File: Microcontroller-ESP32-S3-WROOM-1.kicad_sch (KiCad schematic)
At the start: 8 parts, among them SW1 SW_Push, U1 ESP32-S3-WROOM-1

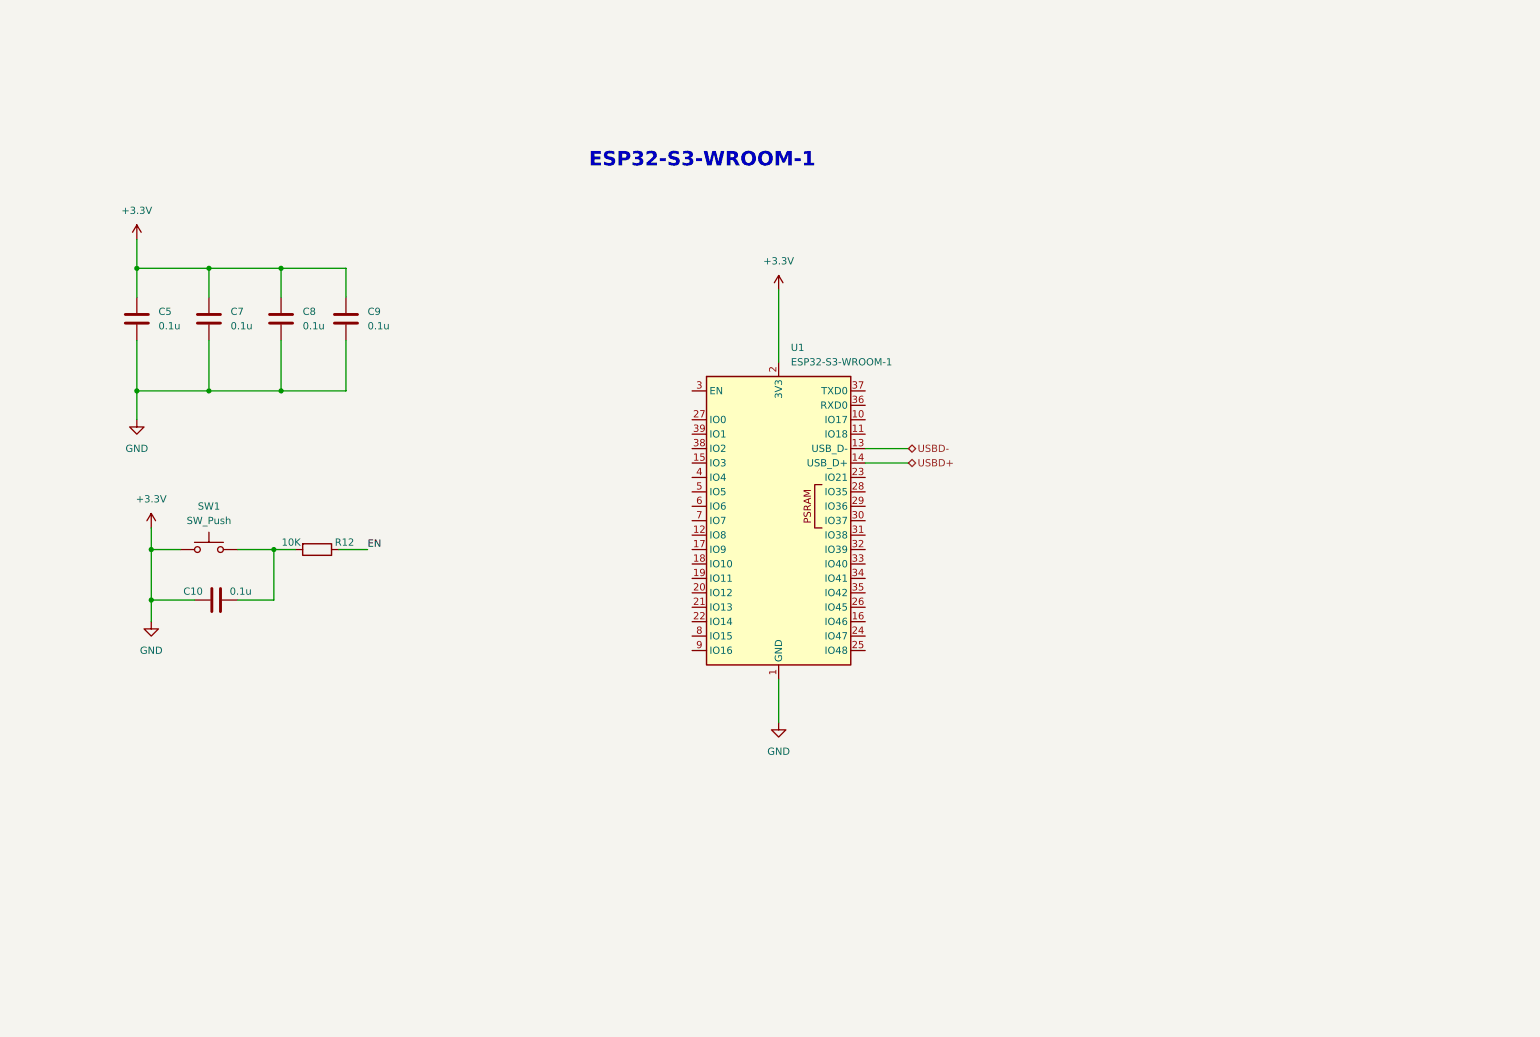
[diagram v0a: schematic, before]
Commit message: feat(schematic): replace capacitor with LED component
Update the ESP32-S3 schematic by replacing a generic capacitor symbol with a specific LED component (LTST-C170KRKT), including updated footprints, properties, and pin configurations.
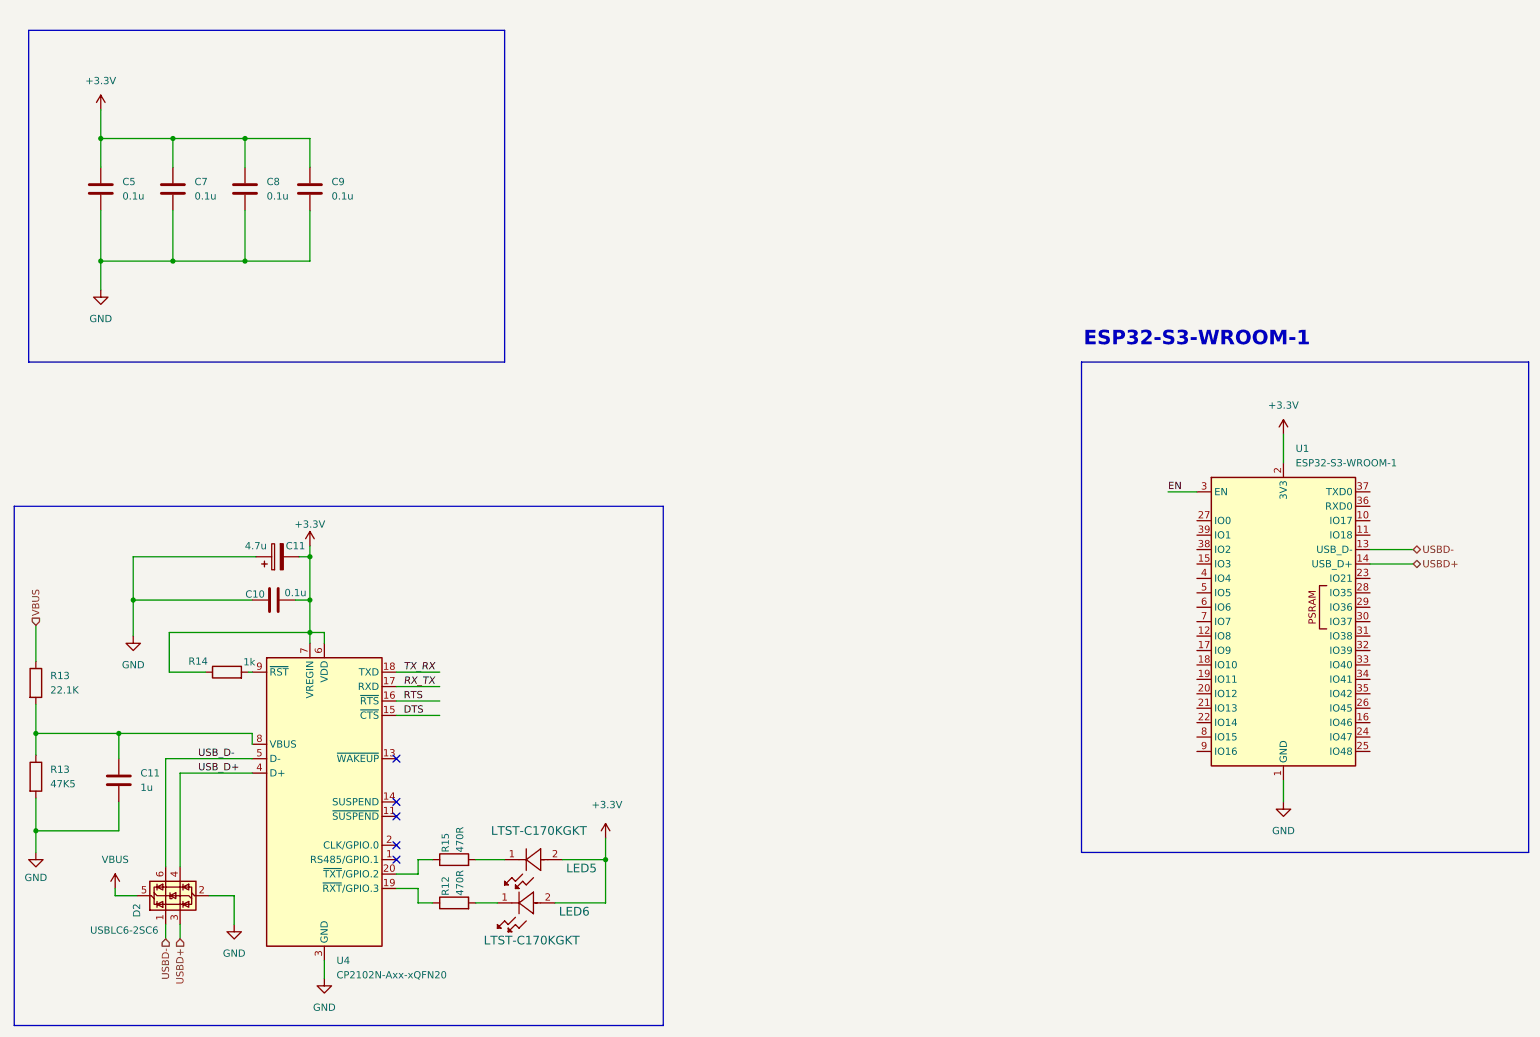
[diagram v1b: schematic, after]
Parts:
- removed SW1: SW_Push, symbol Switch:SW_Push
- added C11: 4.7u, FootPrints:CAPMP3216X180N, symbol Device:C_Polarized
- added C11: 1u, Capacitor_SMD:C_0805_2012Metric, symbol Device:C
- added D2: USBLC6-2SC6, Package_TO_SOT_SMD:SOT-23-6, symbol Power_Protection:USBLC6-2SC6
- added LED5, LED6: LTST-C170KGKT, LED_SMD:LED_0805_2012Metric, symbol 2025-07-01_05-07-46:LTST-C170KRKT
- added R13: 22.1K, Resistor_SMD:R_0805_2012Metric, symbol Device:R
- added R13: 47K5, Resistor_SMD:R_0805_2012Metric, symbol Device:R
- added R14: 1k, Resistor_SMD:R_0805_2012Metric, symbol Device:R
- added R15: 470R, Resistor_SMD:R_0201_0603Metric, symbol Device:R
- added U4: CP2102N-Axx-xQFN20, FootPrints:WFQFN-20, symbol Interface_USB:CP2102N-Axx-xQFN20
- R12: value 10K -> 470R; footprint Resistor_SMD:R_0805_2012Metric -> Resistor_SMD:R_0201_0603Metric; Distributor_link_1 https://eu.mouser.com/ProductDetail/Vishay/CRCW121810K0FKEK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 -> https://eu.mouser.com/ProductDetail/Vishay/CRCW0603470RFKEB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; Distributor_link_2 https://www.digikey.com/en/products/detail/vishay-dale/CRCW121810K0FKEK/28261299 -> https://www.digikey.com/en/products/detail/vishay-dale/CRCW0603470RFKEBC/7925149; LCSC C2144629 -> C4553842; Manufacturer CRCW121810K0FKEK -> Vishay; Manufacturer_part_number Vishay -> CRCW0603470RFKEBC
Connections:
- net +3.3V: now also C10.2, C11.2, LED5.2, LED6.2, R14.1, U4.6 (VDD), U4.7 (VREGIN); no longer C10.1, C5.2, C7.2, C8.2, C9.2, U1.1 (GND), U1.40 (GND), U1.41 (GND)
- net EN: now also U1.3 (EN); no longer R12.1
- net USBD+: now also D2.3 (I/O2)
- net USBD-: now also D2.1 (I/O1)
- net at R12.2: now also LED6.1; no longer C10.2
- new net: R15.1, U4.20 (~{TXT}/GPIO.2)
- new net: LED5.1, R15.2
- new net: C11.1, R13.1, R13.2, U4.8 (VBUS)
- new net: R14.2, U4.9 (~{RST})
- new net: R12.1, U4.19 (~{RXT}/GPIO.3)
- new net DTS: U4.15 (~{CTS})
- new net GND: C10.1, C11.1, C11.2, C5.2, C7.2, C8.2, C9.2, D2.2 (GND), R13.2, U1.1 (GND), U1.40 (GND), U1.41 (GND), U4.12 (GND), U4.21 (GND), U4.3 (GND)
- new net RTS: U4.16 (~{RTS})
- new net RX_TX: U4.17 (RXD)
- new net TX_RX: U4.18 (TXD)
- new net USB_D+: D2.4 (I/O2), U4.4 (D+)
- new net USB_D-: D2.6 (I/O1), U4.5 (D-)
- new net VBUS: D2.5 (VBUS), R13.1
- no-connect marks 0 -> 5
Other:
- moved on the sheet: C5, C7, C8, C9, U1

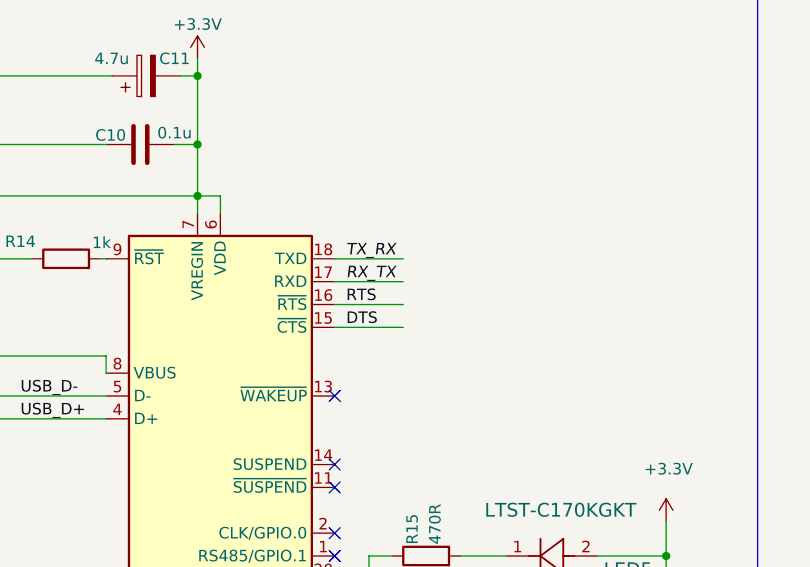
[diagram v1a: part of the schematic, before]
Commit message: feat(schematic): update component properties and label positions
Update capacitor metadata including manufacturer, part numbers, datasheets, and distributor links. Adjust the position of TX/RX labels for better schematic layout.
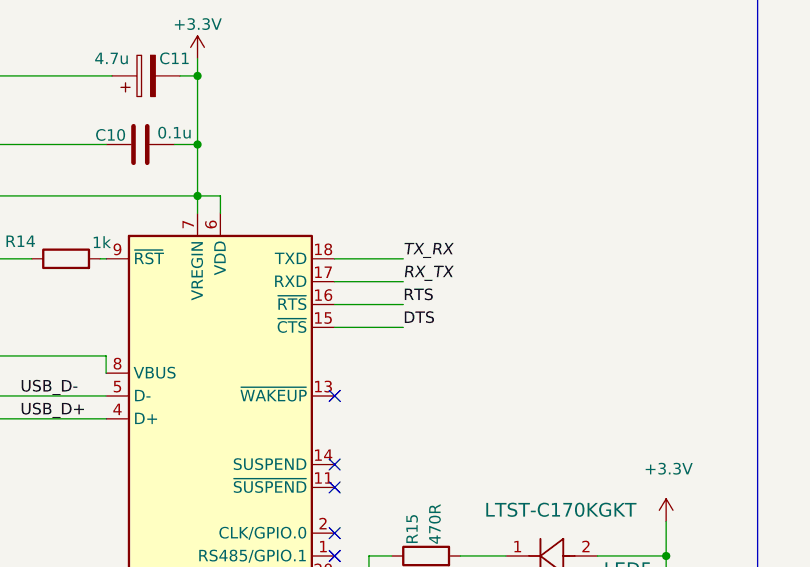
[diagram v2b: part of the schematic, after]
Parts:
- C11: Distributor_link_1 (none) -> https://eu.mouser.com/ProductDetail/Lelon/VES4R7M1VTR-0405?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; Distributor_link_2 (none) -> https://www.digikey.com/en/products/detail/surge/VES4R7M1VT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; LCSC (none) -> C249722; Manufacturer (none) -> Lelon; Manufacturer_part_number (none) -> VES4R7M1VTR-0405
- C11: Distributor_link_1 (none) -> https://eu.mouser.com/ProductDetail/KEMET/C0805X105K8RACTU?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; Distributor_link_2 (none) -> https://www.digikey.com/en/products/detail/kemet/C0805X105K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; LCSC (none) -> C2182388; Manufacturer (none) -> KEMET; Manufacturer_part_number (none) -> C0805X105K8RACTU
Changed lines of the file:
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@@
 	)
 	(label "TX_RX"
-		(at 83.82 130.81 0)
+		(at 90.17 130.81 0)
 		(effects
 			(font
@@
 	)
 	(label "DTS"
-		(at 83.82 138.43 0)
+		(at 90.17 138.43 0)
 		(effects
 			(font
@@
 	)
 	(label "RTS"
-		(at 83.82 135.89 0)
+		(at 90.17 135.89 0)
 		(effects
 			(font
@@
 	)
 	(label "RX_TX"
-		(at 83.82 133.35 0)
+		(at 90.17 133.35 0)
 		(effects
 			(font
@@
 			)
 		)
-		(property "Datasheet" "~"
+		(property "Datasheet" "https://www.lelon.com.tw/upload/prod/154355660662.pdf"
 			(at 61.595 110.49 0)
 			(effects
@@
 			)
 		)
-		(property "Description" "Polarized capacitor"
+		(property "Description" "Aluminium Electrolytic Capacitors - SMD 35 Volts 4.7uF 20% 4x5.3"
 			(at 61.595 110.49 0)
+			(effects
+				(font
+					(size 1.27 1.27)
+				)
+				(hide yes)
+			)
+		)
+		(property "Manufacturer" "Lelon"
+			(at 61.595 110.49 90)
+			(effects
+				(font
+					(size 1.27 1.27)
+				)
+				(hide yes)
+			)
+		)
+		(property "Manufacturer_part_number" "VES4R7M1VTR-0405"
+			(at 61.595 110.49 90)
+			(effects
+				(font
+					(size 1.27 1.27)
+				)
+				(hide yes)
+			)
+		)
+		(property "Distributor_link_1" "https://eu.mouser.com/ProductDetail/Lelon/VES4R7M1VTR-0405?qs=ZaMXuU%252B6JZYpwK4%252Bl1EUyg%3D%3D"
+			(at 61.595 110.49 90)
+			(effects
+				(font
+					(size 1.27 1.27)
+				)
+				(hide yes)
+			)
+		)
+		(property "Distributor_link_2" "https://www.digikey.com/en/products/detail/surge/VES4R7M1VTR-0405S/21295607?s=N4IgTCBcDaIGoFEDKAWASgdgLIEY4BU0BaABhRIFYQBdAXyA"
+			(at 61.595 110.49 90)
+			(effects
+				(font
+					(size 1.27 1.27)
+				)
+				(hide yes)
+			)
+		)
+		(property "LCSC" "C249722"
+			(at 61.595 110.49 90)
 			(effects
 				(font
@@
 			)
 		)
-		(property "Datasheet" "~"
+		(property "Datasheet" "https://eu.mouser.com/datasheet/3/72/1/C0805X105K8RACTU.pdf"
 			(at 33.655 149.86 0)
 			(effects
@@
 			)
 		)
-		(property "Description" "Unpolarized capacitor"
+		(property "Description" "Multilayer Ceramic Capacitors MLCC - SMD/SMT 10V 1uF X7R 0805 10% Flex Soft"
 			(at 33.655 149.86 0)
 			(effects
+				(font
+					(size 1.27 1.27)
+				)
+				(hide yes)
+			)
+		)
+		(property "Manufacturer" "KEMET"
+			(at 33.655 149.86 0)
+			(effects
+				(font
+					(size 1.27 1.27)
+				)
+				(hide yes)
+			)
+		)
+		(property "Manufacturer_part_number" "C0805X105K8RACTU"
+			(at 33.655 149.86 0)
+			(effects
+				(font
+					(size 1.27 1.27)
+				)
+				(hide yes)
+			)
+		)
+		(property "Distributor_link_1" "https://eu.mouser.com/ProductDetail/KEMET/C0805X105K8RACTU?qs=p6yRp5s%252B%2FXRBx6%252BCsmrxtg%3D%3D"
+			(at 33.655 149.86 0)
+			(effects
+				(font
+					(size 1.27 1.27)
+				)
+				(hide yes)
+			)
+		)
+		(property "Distributor_link_2" "https://www.digikey.com/en/products/detail/kemet/C0805X105K8RACTU/1842270?s=N4IgTCBcDaIMIAYAcCCsANAjGg0kgSgIJwAqAqiALoC%2BQA"
+			(at 33.655 149.86 0)
+			(effects
+				(font
+					(size 1.27 1.27)
+				)
+				(hide yes)
+			)
+		)
+		(property "LCSC" "C2182388"
+			(at 33.655 149.86 0)
+			(effects
